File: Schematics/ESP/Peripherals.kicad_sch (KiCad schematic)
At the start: 38 parts, among them J12 Conn_01x02_Pin, J3 Conn_01x04_Pin, J4 Conn_01x02_Male, J5 Conn_01x02_Male, J6 Screw_Terminal_01x02 Fan, Q17 IRF540N, Q3 AO3401A, U4 DRV8871DDA, U5 LM2596S-5, U6 DRV8871DDA

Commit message: Can Pull
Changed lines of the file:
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@@
     (effects (font (size 1.27 1.27)) (justify left bottom))
   )
-  (text "P-channel MOSFET for \nreverse polarity protection" (at 54.61 39.37 0)
+  (text "P-channel MOSFET for \nreverse polarity protection" (at 45.72 38.1 0)
     (effects (font (size 1.27 1.27)) (justify left bottom))
   )
@@
       (effects (font (size 1.27 1.27)))
     )
-    (property "Value" "Conn_01x04_Pin" (at 257.175 146.05 0)
-      (effects (font (size 1.27 1.27)))
-    )
+    (property "Value" "Conn_01x04_Pin" (at 260.35 144.78 0)
+      (effects (font (size 1.27 1.27)))
+    )

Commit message: Can Pull
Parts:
- added C10: 680u, Capacitor_THT:CP_Radial_D10.0mm_P5.00mm, symbol Device:C_Polarized_Small
- added C8: 10n, Capacitor_SMD:C_1206_3216Metric_Pad1.33x1.80mm_HandSolder, symbol Device:C_Small
- added D5: 1N4001, Diode_THT:D_DO-41_SOD81_P10.16mm_Horizontal, symbol Diode:1N4001
- R4: value 10k -> 6.2k; digikey link https://www.digikey.fi/en/products/detail/yageo/RC1206FR-07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 -> https://www.digikey.fi/en/products/detail/yageo/RC1206JR-07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
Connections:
- net Battery level: now also C8.1
- net Battery+: now also C10.1, Q3.2 (S), U5.1 (VIN), C10.1, D5.1 (K); no longer F1.1
- net GND: now also C10.2, C8.2
- net at F1.2, J6.2 (Pin_2): now also D5.2 (A)
- new net +12V: F1.1
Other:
- note added: "(4.2*3 V) * (6.2k / (6.2k+(2*10k)) = 2.9816 V"
- moved on the sheet: F1, J6

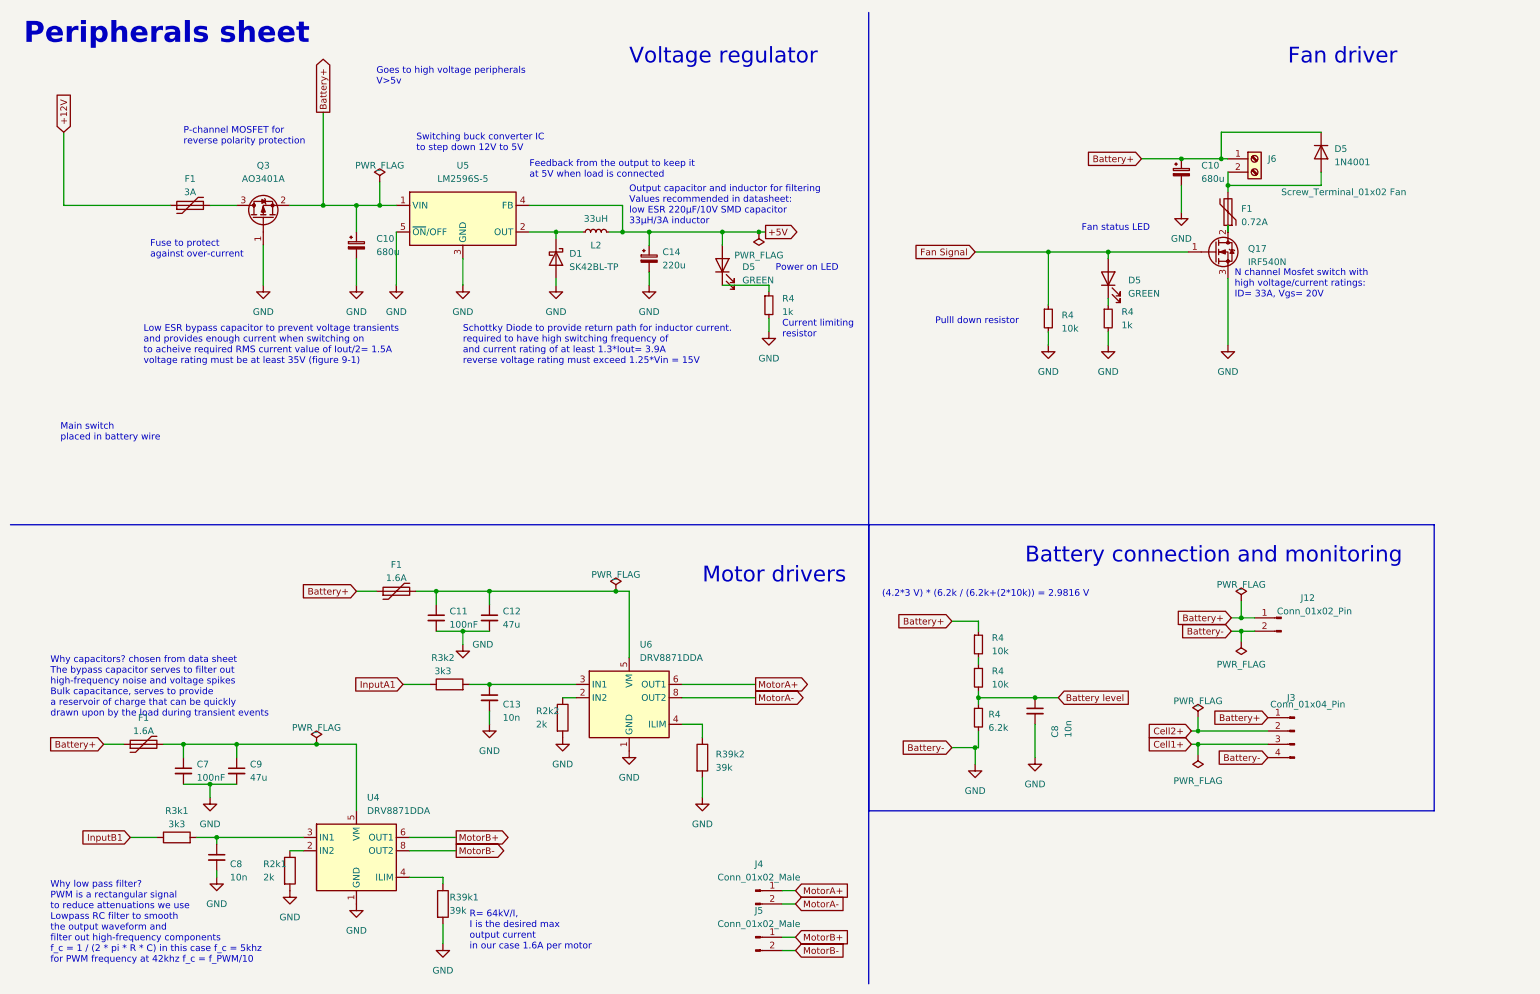
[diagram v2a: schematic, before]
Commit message: PCB layout done no wiring
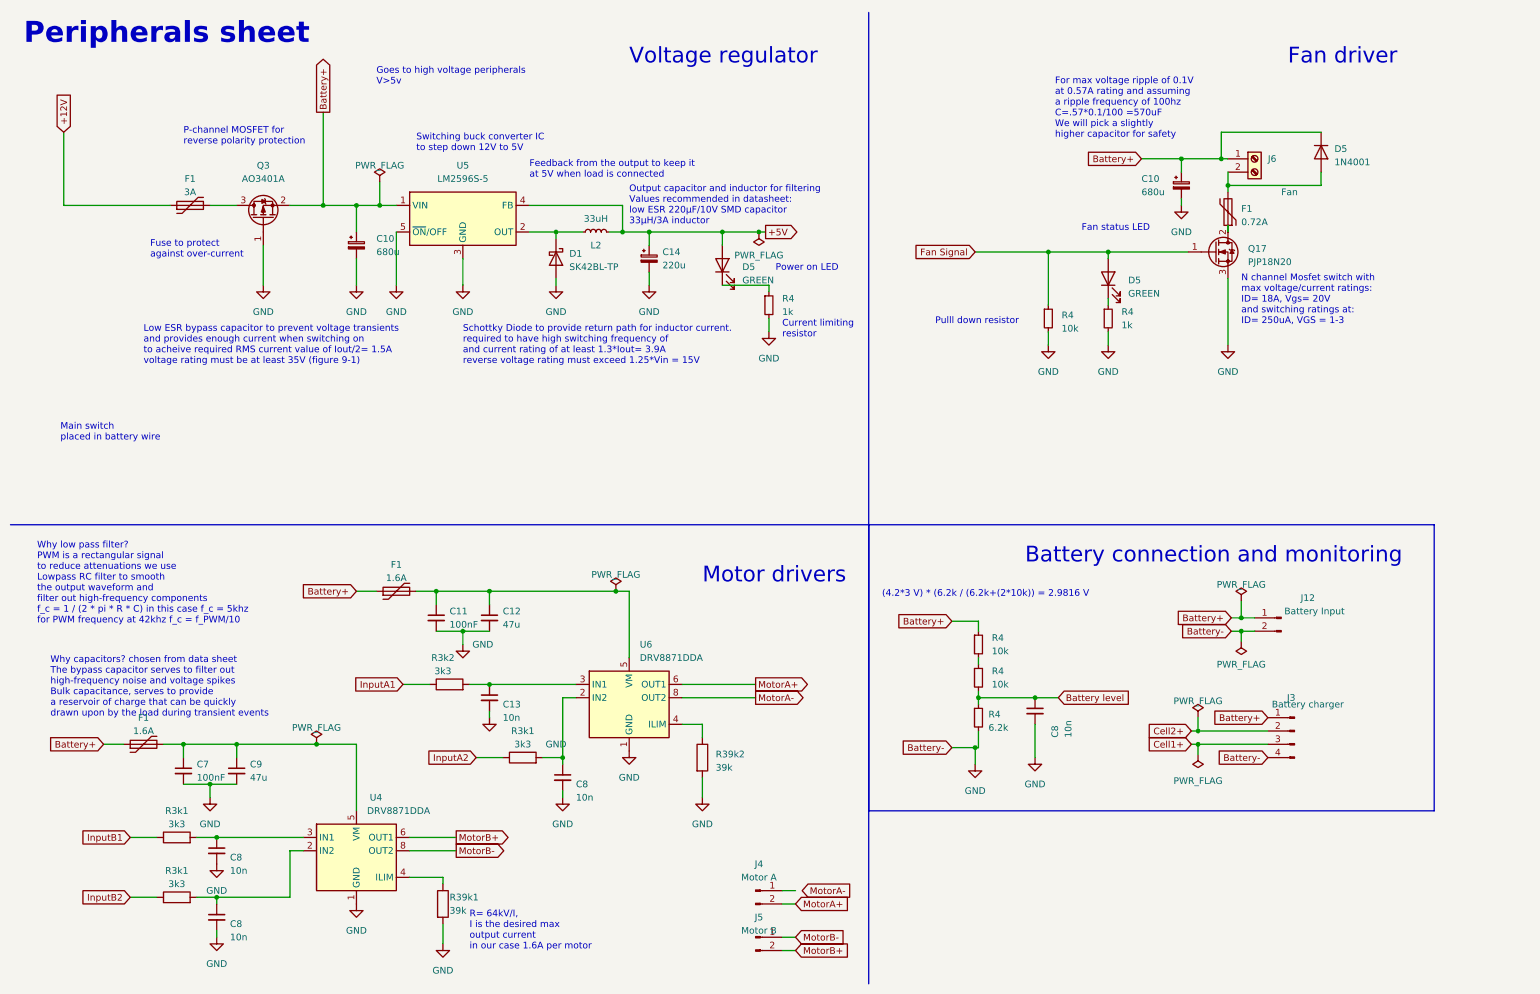
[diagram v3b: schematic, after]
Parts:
- removed R2k1, R2k2: 2k, Resistor_SMD:R_1206_3216Metric_Pad1.30x1.75mm_HandSolder, symbol Device:R
- added C8 (x2): 10n, Capacitor_SMD:C_1206_3216Metric_Pad1.33x1.80mm_HandSolder, symbol Device:C_Small
- added R3k1 (x2): 3k3, Resistor_SMD:R_1206_3216Metric_Pad1.30x1.75mm_HandSolder, symbol Device:R
- J12: value Conn_01x02_Pin -> Battery Input
- J3: value Conn_01x04_Pin -> Battery charger
- J4: value Conn_01x02_Male -> Motor A; footprint Connector_PinHeader_1.27mm:PinHeader_1x02_P1.27mm_Horizontal -> Connector_PinHeader_2.54mm:PinHeader_1x02_P2.54mm_Horizontal
- J5: value Conn_01x02_Male -> Motor B; footprint Connector_PinHeader_1.27mm:PinHeader_1x02_P1.27mm_Horizontal -> Connector_PinHeader_2.54mm:PinHeader_1x02_P2.54mm_Horizontal
- J6: value Screw_Terminal_01x02 Fan -> Fan
- Q17: value IRF540N -> PJP18N20; Price 1,44 -> 1.22; digikey link https://www.digikey.fi/en/products/detail/infineon-technolo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 -> https://www.digikey.fi/en/products/detail/panjit-internatio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
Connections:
- net GND: now also C8.2, C8.2
- net MotorA+: now also J4.2 (Pin_2); no longer J4.1 (Pin_1)
- net MotorA-: no longer J4.2 (Pin_2)
- net MotorB+: now also J5.2 (Pin_2); no longer J5.1 (Pin_1)
- net MotorB-: now also J5.1 (Pin_1); no longer J5.2 (Pin_2)
- net at U6.2 (IN2): now also C8.1, R3k1.2
- net at U4.2 (IN2): now also C8.1, R3k1.2
- new net InputA2: R3k1.1
- new net InputB2: R3k1.1
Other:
- note added: "For max voltage ripple of 0.1V at 0.57A rating and assuming a ripple frequency of 100hz C=.57*0.1/100 =570uF We will pick a slightly higher capacitor for safety"
- note added: "N channel Mosfet switch with max voltage/current ratings: ID= 18A, Vgs= 20V and switching ratings at: ID= 250uA, VGS = 1-3"
- note removed: "N channel Mosfet switch with high voltage/current ratings: ID= 33A, Vgs= 20V"
- moved on the sheet: C10, C8

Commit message: PCB layout done no wiring
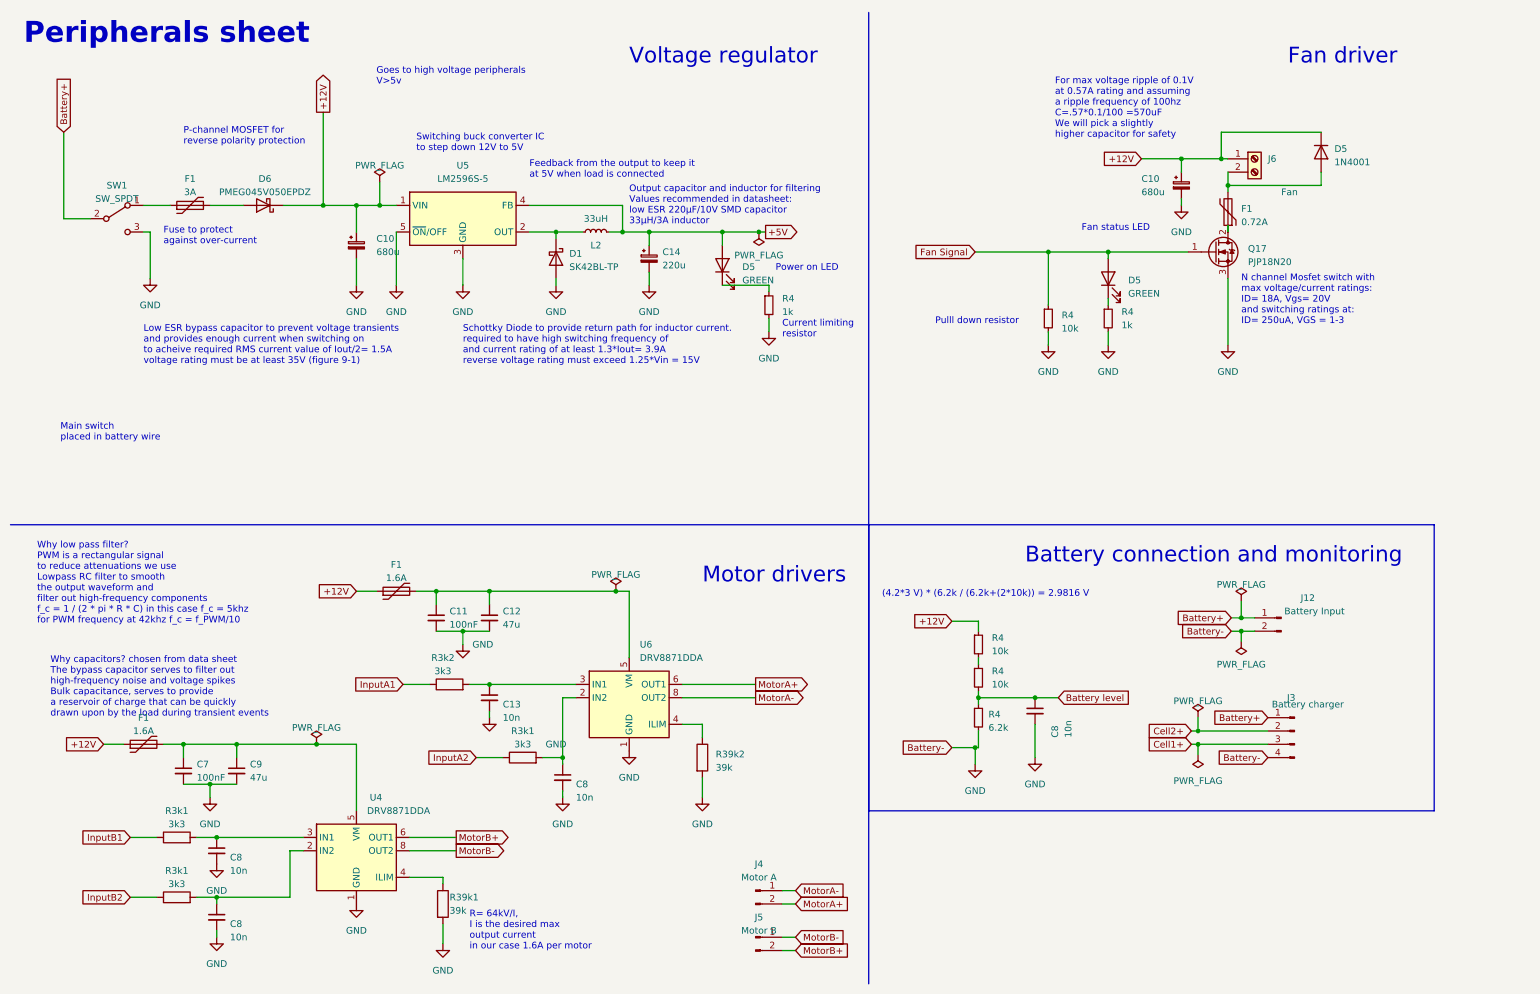
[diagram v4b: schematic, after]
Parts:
- removed Q3: AO3401A, Package_TO_SOT_SMD:SOT-23, symbol Transistor_FET:AO3401A
- added D6: PMEG045V050EPDZ, Diode_SMD:D_SMB, symbol Device:D_Schottky
- added SW1: SW_SPDT, 500SSP1S1M6QEA:SW_500SSP1S1M6QEA, symbol Switch:SW_SPDT
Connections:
- net +12V: now also C10.1, C10.1, D5.1 (K), F1.1, F1.1, J6.1 (Pin_1), R4.1, U5.1 (VIN), D6.1 (K); no longer F1.1
- net Battery+: now also SW1.2 (B); no longer C10.1, C10.1, D5.1 (K), F1.1, F1.1, J6.1 (Pin_1), R4.1, U5.1 (VIN)
- net GND: now also SW1.3 (C)
- net MotorA-: now also J4.1 (Pin_1)
- net at F1.2: now also D6.2 (A)
- new net: F1.1, SW1.1 (A)

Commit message: did some stuff
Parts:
- F1: value 3A -> 5A
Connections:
- net Battery+: no longer J3.1 (Pin_1)
- net GND: no longer J3.4 (Pin_4)
- new net Cell1-: J3.4 (Pin_4)
- new net Cell3+: J3.1 (Pin_1)
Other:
- note added: "Diode for reverse polarity protection"
- note removed: "P-channel MOSFET for reverse polarity protection"
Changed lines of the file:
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@@
   (junction (at 52.07 181.61) (diameter 0) (color 0 0 0 0)
   )
-  (junction (at 239.395 152.4) (diameter 0) (color 0 0 0 0)
-  )
   (junction (at 83.185 49.53) (diameter 0) (color 0 0 0 0)
   )
@@
   (junction (at 99.06 130.81) (diameter 0) (color 0 0 0 0)
   )
-  (junction (at 239.395 149.86) (diameter 0) (color 0 0 0 0)
-  )
   (wire (pts (xy 64.77 49.53) (xy 72.39 49.53))
     (stroke (width 0) (type default))
@@
     (stroke (width 0) (type default))
   )
-  (wire (pts (xy 239.395 147.32) (xy 239.395 149.86))
-    (stroke (width 0) (type default))
-  )
   (wire (pts (xy 245.11 54.61) (xy 245.11 53.34))
     (stroke (width 0) (type default))
@@
     (stroke (width 0) (type default))
   )
-  (wire (pts (xy 238.125 152.4) (xy 239.395 152.4))
-    (stroke (width 0) (type default))
-  )
   (wire (pts (xy 99.06 59.69) (xy 99.06 64.77))
     (stroke (width 0) (type default))
@@
     (stroke (width 0) (type default))
   )
-  (wire (pts (xy 239.395 152.4) (xy 252.73 152.4))
-    (stroke (width 0) (type default))
-  )
   (wire (pts (xy 95.25 177.8) (xy 95.25 179.07))
     (stroke (width 0) (type default))
@@
     (stroke (width 0) (type default))
   )
-  (wire (pts (xy 239.395 154.305) (xy 239.395 152.4))
-    (stroke (width 0) (type default))
-  )
   (wire (pts (xy 78.74 123.19) (xy 82.55 123.19))
     (stroke (width 0) (type default))
@@
     (stroke (width 0) (type default))
   )
-  (wire (pts (xy 238.125 149.86) (xy 239.395 149.86))
-    (stroke (width 0) (type default))
-  )
   (wire (pts (xy 129.54 49.53) (xy 129.54 54.61))
     (stroke (width 0) (type default))
@@
   )
   (wire (pts (xy 160.02 191.77) (xy 162.56 191.77))
-    (stroke (width 0) (type default))
-  )
-  (wire (pts (xy 239.395 149.86) (xy 252.73 149.86))
     (stroke (width 0) (type default))
   )
@@
     (effects (font (size 1.27 1.27)) (justify left bottom))
   )
-  (text "P-channel MOSFET for \nreverse polarity protection" (at 45.72 38.1 0)
+  (text "Diode for reverse polarity\nprotection" (at 47.625 40.64 0)
     (effects (font (size 1.27 1.27)) (justify left bottom))
   )
@@
     (effects (font (size 1.27 1.27)) (justify left bottom))
   )
-  (global_label "Battery+" (shape input) (at 252.73 147.32 180) (fields_autoplaced)
+  (global_label "Cell3+" (shape input) (at 252.73 147.32 180) (fields_autoplaced)
     (effects (font (size 1.27 1.27)) (justify right))
-    (property "Intersheetrefs" "${INTERSHEET_REFS}" (at 241.539 147.32 0)
+    (property "Intersheetrefs" "${INTERSHEET_REFS}" (at 243.3533 147.32 0)
       (effects (font (size 1.27 1.27)) (justify right) hide)
     )
@@
     )
   )
-  (global_label "Cell1+" (shape input) (at 238.125 152.4 180) (fields_autoplaced)
+  (global_label "Cell1+" (shape input) (at 252.73 152.4 180) (fields_autoplaced)
     (effects (font (size 1.27 1.27)) (justify right))
-    (property "Intersheetrefs" "${INTERSHEET_REFS}" (at 228.7483 152.4 0)
+    (property "Intersheetrefs" "${INTERSHEET_REFS}" (at 243.3533 152.4 0)
       (effects (font (size 1.27 1.27)) (justify right) hide)
     )
@@
     )
   )
-  (global_label "Cell2+" (shape input) (at 238.125 149.86 180) (fields_autoplaced)
+  (global_label "Cell2+" (shape input) (at 252.73 149.86 180) (fields_autoplaced)
     (effects (font (size 1.27 1.27)) (justify right))
-    (property "Intersheetrefs" "${INTERSHEET_REFS}" (at 228.7483 149.86 0)
+    (property "Intersheetrefs" "${INTERSHEET_REFS}" (at 243.3533 149.86 0)
       (effects (font (size 1.27 1.27)) (justify right) hide)
     )
@@
     )
   )
-  (global_label "Battery-" (shape input) (at 252.73 154.94 180) (fields_autoplaced)
+  (global_label "Cell1-" (shape input) (at 252.73 154.94 180) (fields_autoplaced)
     (effects (font (size 1.27 1.27)) (justify right))
-    (property "Intersheetrefs" "${INTERSHEET_REFS}" (at 241.539 154.94 0)
+    (property "Intersheetrefs" "${INTERSHEET_REFS}" (at 243.3533 154.94 0)
       (effects (font (size 1.27 1.27)) (justify right) hide)
     )
@@
         (path "/b616d203-cf5c-462f-b907-860a8573592a/9ad1e8da-d13f-4a6e-8aa2-8655a1d493de"
           (reference "F4") (unit 1)
-        )
-      )
-    )
-  )
-  (symbol (lib_id "power:PWR_FLAG") (at 239.395 154.305 180) (unit 1)
-    (in_bom yes) (on_board yes) (dnp no) (fields_autoplaced)
-    (property "Reference" "#FLG04" (at 239.395 156.21 0)
-      (effects (font (size 1.27 1.27)) hide)
-    )
-    (property "Value" "PWR_FLAG" (at 239.395 159.385 0)
-      (effects (font (size 1.27 1.27)))
-    )
-    (property "Footprint" "" (at 239.395 154.305 0)
-      (effects (font (size 1.27 1.27)) hide)
-    )
-    (property "Datasheet" "~" (at 239.395 154.305 0)
-      (effects (font (size 1.27 1.27)) hide)
-    )
-    (pin "1")
-    (instances
-      (project "ESP"
-        (path "/b616d203-cf5c-462f-b907-860a8573592a/9ad1e8da-d13f-4a6e-8aa2-8655a1d493de"
-          (reference "#FLG04") (unit 1)
         )
       )
@@
     )
   )
-  (symbol (lib_id "power:PWR_FLAG") (at 239.395 147.32 0) (unit 1)
-    (in_bom yes) (on_board yes) (dnp no) (fields_autoplaced)
-    (property "Reference" "#FLG03" (at 239.395 145.415 0)
-      (effects (font (size 1.27 1.27)) hide)
-    )
-    (property "Value" "PWR_FLAG" (at 239.395 144.145 0)
-      (effects (font (size 1.27 1.27)))
-    )
-    (property "Footprint" "" (at 239.395 147.32 0)
-      (effects (font (size 1.27 1.27)) hide)
-    )
-    (property "Datasheet" "~" (at 239.395 147.32 0)
-      (effects (font (size 1.27 1.27)) hide)
-    )
-    (pin "1")
-    (instances
-      (project "ESP"
-        (path "/b616d203-cf5c-462f-b907-860a8573592a/9ad1e8da-d13f-4a6e-8aa2-8655a1d493de"
-          (reference "#FLG03") (unit 1)
-        )
-      )
-    )
-  )
   (symbol (lib_id "power:GND") (at 116.84 64.77 0) (unit 1)
     (in_bom yes) (on_board yes) (dnp no) (fields_autoplaced)
@@
       (effects (font (size 1.27 1.27)))
     )
-    (property "Value" "3A" (at 46.99 46.99 90)
-      (effects (font (size 1.27 1.27)))
-    )
+    (property "Value" "5A" (at 46.99 46.99 90)
+      (effects (font (size 1.27 1.27)))
+    )
